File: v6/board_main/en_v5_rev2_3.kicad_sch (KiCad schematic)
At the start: 28 parts, among them M1 SISS23DN, M2 SISS23DN, U4 PAC1934, U5 PAC1934

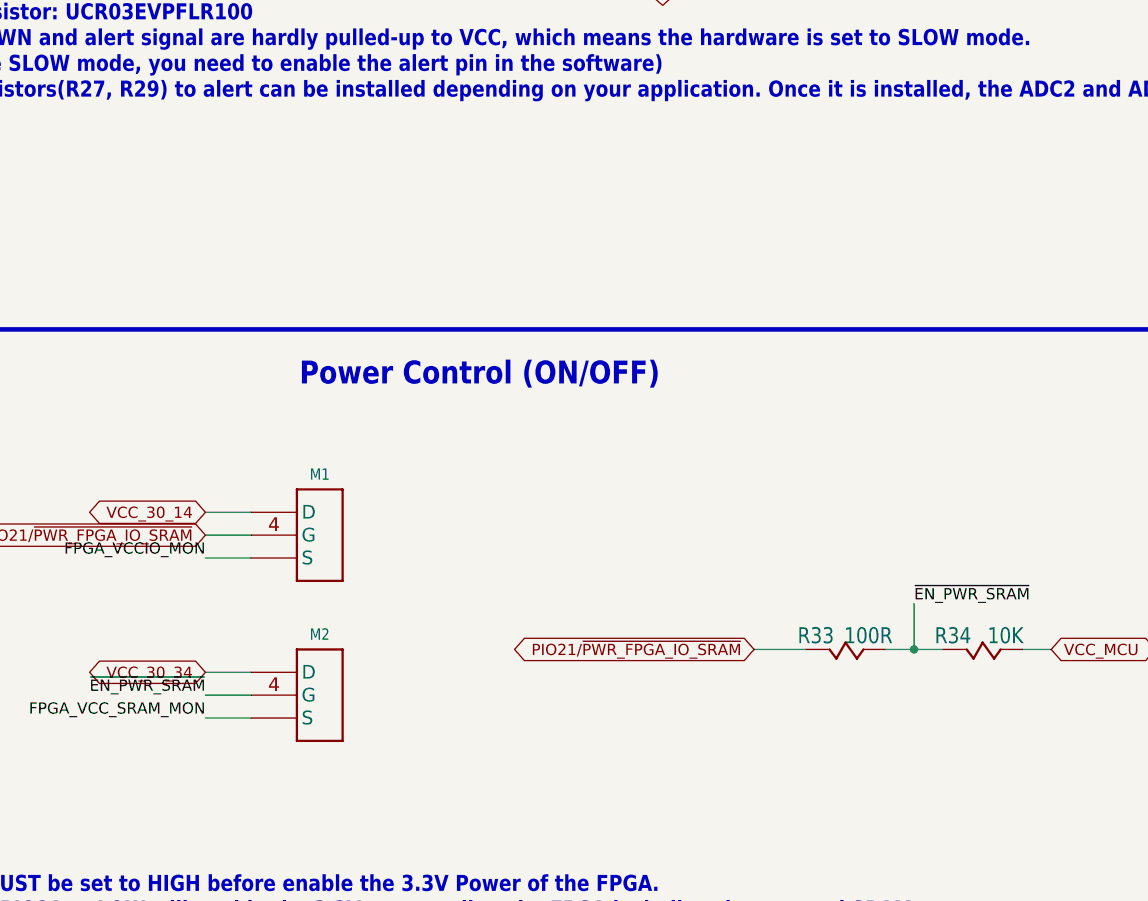
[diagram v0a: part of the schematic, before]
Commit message: Rephrasing ENV5 design
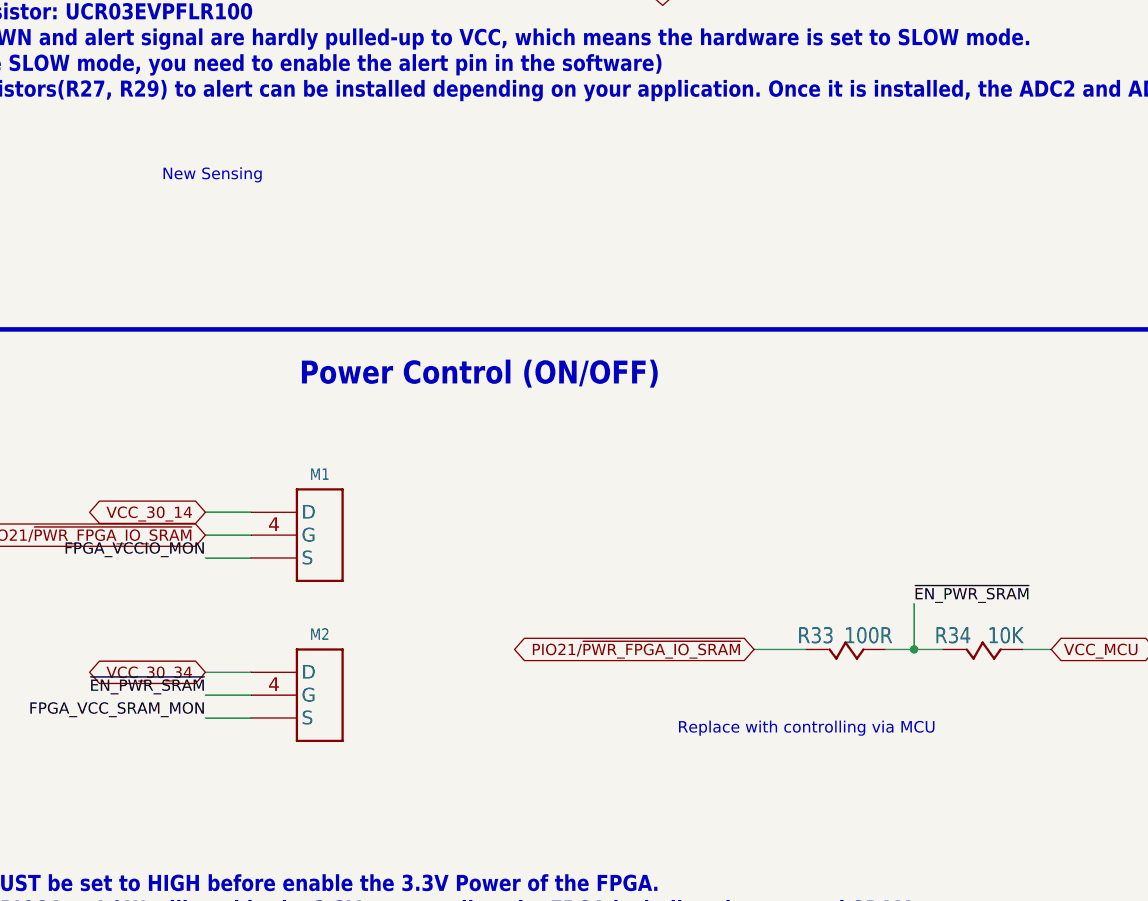
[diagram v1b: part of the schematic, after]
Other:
- note added: "New Sensing"
- note added: "Replace with controlling via MCU"
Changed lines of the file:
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@@
 	(generator_version "9.0")
 	(paper "User" 304.648 217.322)
+	(text "New Sensing"
+		(exclude_from_sim no)
+		(at 58.674 106.68 0)
+		(effects
+			(font
+				(size 1.27 1.27)
+			)
+			(justify left top)
+		)
+	)
 	(text "I2C Pullup Resistors"
 		(exclude_from_sim no)
@@
 			)
 		)
+	)
+	(text "Replace with controlling via MCU"
+		(exclude_from_sim no)
+		(at 130.302 168.91 0)
+		(effects
+			(font
+				(size 1.27 1.27)
+			)
+		)

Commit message: ENV6 (test): Changes after first review
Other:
- note added: "Adress = 0x11"
- note added: "Adress = 0x12"
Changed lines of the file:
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@@
+		)
+	)
+	(text "Adress = 0x11"
+		(exclude_from_sim no)
+		(at 72.136 37.084 0)
+		(effects
+			(font
+				(size 1.27 1.27)
+			)
 		)
 	)
@@
 		)
 	)
+	(text "Adress = 0x12"
+		(exclude_from_sim no)
+		(at 199.898 38.862 0)
+		(effects
+			(font
+				(size 1.27 1.27)
+			)
+		)
+	)
